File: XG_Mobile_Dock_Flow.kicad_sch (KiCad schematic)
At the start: 22 parts, among them J1 5-1775443-8, J13 39300240, J14 469911008, J17 8730, J2 20455-040E-76, J3 20455-040E-76, J4 3-2362375-4, J5 USB_C_Receptacle, SW1 SW_Push, U1 DS160PR410RNQR, U2 DS160PR410RNQR

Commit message: added more schematic
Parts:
- added C1, C10, C11, C12, C13, C14, C15, C16, C2, C3, C4, C5, C6, C7, C8, C9: 0.22μF, Capacitor_SMD:C_0201_0603Metric, symbol Device:C
- added C17, C18, C19, C20, C22, C23, C24, C25: 0.1μF, Capacitor_SMD:C_0201_0603Metric, symbol Device:C
- added C21, C26: 1μF, Capacitor_SMD:C_0201_0603Metric, symbol Device:C
- added R64, R65: 1k, Resistor_SMD:R_0402_1005Metric, symbol Device:R
- added R66, R67, R68, R69: 59k, Resistor_SMD:R_0402_1005Metric, symbol Device:R
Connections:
- net U1_VDD0 is gone; now on net +3V3: U1.31 (VDD)
- net U1_VDD1 is gone; now on net +3V3: U1.34 (VDD)
- net U1_VDD2 is gone; now on net +3V3: U1.35 (VDD)
- net U1_VDD3 is gone; now on net +3V3: U1.38 (VDD)
- net U2_VDD0 is gone; now on net +3V3: U2.31 (VDD)
- net U2_VDD1 is gone; now on net +3V3: U2.34 (VDD)
- net U2_VDD2 is gone; now on net +3V3: U2.35 (VDD)
- net U2_VDD3 is gone; now on net +3V3: U2.38 (VDD)
- net +3V3: now also C17.2, C18.2, C19.2, C20.2, C21.2, C22.2, C23.2, C24.2, C25.2, C26.2
- net GND: now also U1.21 (PWDN1), U1.25 (PWDN2), U1.41 (GND), U2.21 (PWDN1), U2.25 (PWDN2), U2.41 (GND), C17.1, C18.1, C19.1, C20.1, C21.1, C22.1, C23.1, C24.1, C25.1, C26.1, R64.1, R65.1, R66.1, R67.1, R68.1, R69.1
- net HSO0N: now also C2.2
- net HSO0P: now also C1.2
- net HSO1N: now also C4.2
- net HSO1P: now also C3.2
- net HSO2N: now also C6.2
- net HSO2P: now also C5.2
- net HSO3N: now also C8.2
- net HSO3P: now also C7.2
- net HSO4N: now also C10.2
- net HSO4P: now also C9.2
- net HSO5N: now also C12.2
- net HSO5P: now also C11.2
- net HSO6N: now also C14.2
- net HSO6P: now also C13.2
- net HSO7N: now also C16.2
- net HSO7P: now also C15.2
- net HSOT0N: now also C2.1
- net HSOT0P: now also C1.1
- net HSOT1N: now also C4.1
- net HSOT1P: now also C3.1
- net HSOT2N: now also C6.1
- net HSOT2P: now also C5.1
- net HSOT3N: now also C8.1
- net HSOT3P: now also C7.1
- net HSOT4N: now also C10.1
- net HSOT4P: now also C9.1
- net HSOT5N: now also C12.1
- net HSOT5P: now also C11.1
- net HSOT6N: now also C14.1
- net HSOT6P: now also C13.1
- net HSOT7N: now also C16.1
- net HSOT7P: now also C15.1
- net at U2.2 (EN_SMB): now also R65.2
- net at U2.6 (EQ1_ADDR1): now also R66.2
- net at U2.7 (EQ0_ADDR0): now also R67.2
- net at U1.2 (EN_SMB): now also R64.2
- net at U1.6 (EQ1_ADDR1): now also R68.2
- net at U1.7 (EQ0_ADDR0): now also R69.2
- no-connect marks 0 -> 14
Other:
- moved on the sheet: J14, U2

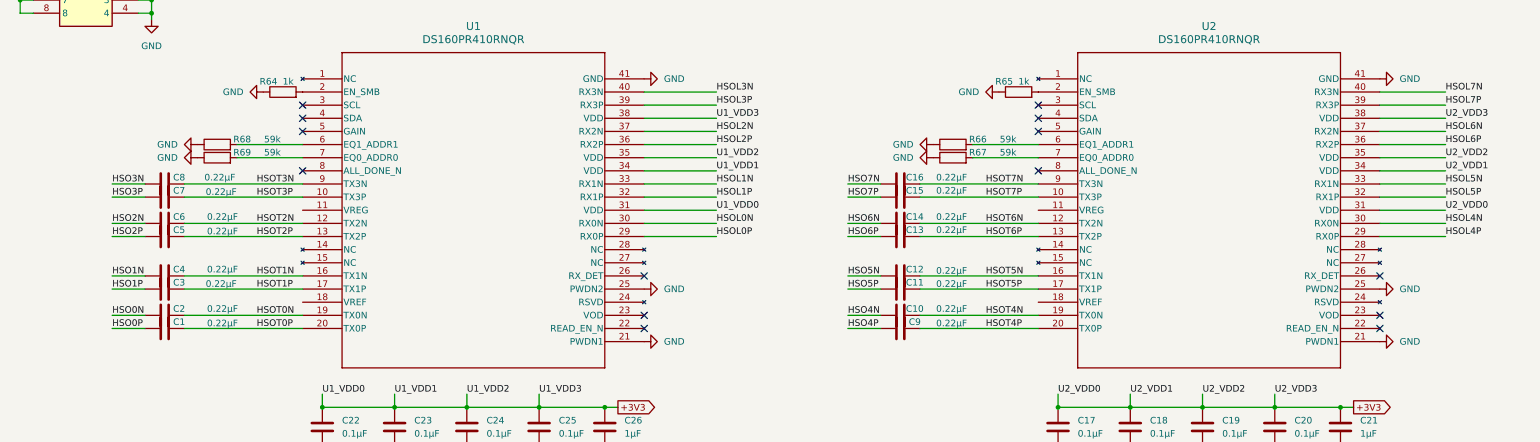
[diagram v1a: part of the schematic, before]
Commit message: added more things to the schematic for proper wiring of open pins with high and low resistors
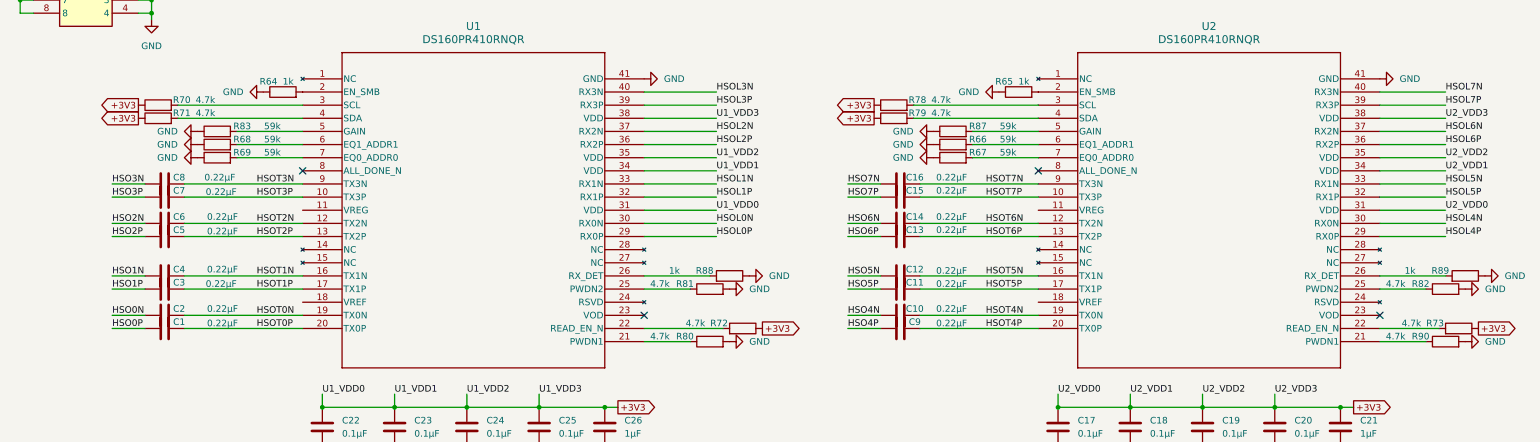
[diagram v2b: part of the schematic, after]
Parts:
- added R70, R71, R72, R73, R78, R79, R80, R81, R82, R90: 4.7k, Resistor_SMD:R_0402_1005Metric, symbol Device:R
- added R83, R87: 59k, Resistor_SMD:R_0402_1005Metric, symbol Device:R
- added R88, R89: 1k, Resistor_SMD:R_0402_1005Metric, symbol Device:R
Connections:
- net +3V3: now also R70.1, R71.1, R72.1, R73.1, R78.1, R79.1
- net GND: now also R80.2, R81.2, R82.2, R83.1, R87.1, R88.1, R89.1, R90.2; no longer U1.21 (PWDN1), U1.25 (PWDN2), U2.21 (PWDN1), U2.25 (PWDN2)
- net at U2.22 (READ_EN_N): now also R73.2
- net at U2.26 (RX_DET): now also R89.2
- net at U2.3 (SCL): now also R78.2
- net at U2.4 (SDA): now also R79.2
- net at U2.5 (GAIN): now also R87.2
- net at U1.22 (READ_EN_N): now also R72.2
- net at U1.26 (RX_DET): now also R88.2
- net at U1.3 (SCL): now also R70.2
- net at U1.4 (SDA): now also R71.2
- net at U1.5 (GAIN): now also R83.2
- new net: R82.1, U2.25 (PWDN2)
- new net: R90.1, U2.21 (PWDN1)
- new net: R80.1, U1.21 (PWDN1)
- new net: R81.1, U1.25 (PWDN2)
- no-connect marks 14 -> 4

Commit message: almost finished everything
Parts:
- added C27, C28, C29, C30: 0.1μF, Capacitor_SMD:C_0201_0603Metric, symbol Device:C
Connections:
- net GND: now also C27.2, C28.2, C29.2, C30.2
- net at U2.11 (VREG): now also C30.1
- net at U2.18 (VREF): now also C29.1
- net at U1.11 (VREG): now also C27.1
- net at U1.18 (VREF): now also C28.1
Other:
- moved on the sheet: C10, C11, C12, C13, C14, C15, C16, C17, C18, C19, C20, C21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

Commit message: more preparations for building the board
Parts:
- C1, C10, C11, C12, C13, C14, C15, C16, C2, C3, C4, C5, C6, C7, C8, C9: value 0.22μF -> 220nF
- C17, C18, C19, C20, C22, C23, C24, C25: value 0.1μF -> 100nF
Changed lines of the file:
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@@
 			)
 		)
-		(property "Value" "0.22μF"
+		(property "Value" "220nF"
 			(at 210.566 235.204 90)
 			(effects
@@
 			)
 		)
-		(property "Value" "0.22μF"
+		(property "Value" "220nF"
 			(at 62.992 217.424 90)
 			(effects
@@
 			)
 		)
-		(property "Value" "0.22μF"
+		(property "Value" "220nF"
 			(at 63.246 242.824 90)
 			(effects
@@
 			)
 		)
-		(property "Value" "0.22μF"
+		(property "Value" "220nF"
 			(at 210.566 240.03 90)
 			(effects
@@
 			)
 		)
-		(property "Value" "0.22μF"
+		(property "Value" "220nF"
 			(at 63.246 222.25 90)
 			(effects
@@
 			)
 		)
-		(property "Value" "0.22μF"
+		(property "Value" "220nF"
 			(at 210.566 242.824 90)
 			(effects
@@
 			)
 		)
-		(property "Value" "0.1μF"
+		(property "Value" "100nF"
 			(at 100.33 264.1599 0)
 			(effects
@@
 			)
 		)
-		(property "Value" "0.1μF"
+		(property "Value" "100nF"
 			(at 114.3 264.1599 0)
 			(effects
@@
 			)
 		)
-		(property "Value" "0.1μF"
+		(property "Value" "100nF"
 			(at 128.27 264.1599 0)
 			(effects
@@
 			)
 		)
-		(property "Value" "0.1μF"
+		(property "Value" "100nF"
 			(at 276.86 264.1599 0)
 			(effects
@@
 			)
 		)
-		(property "Value" "0.22μF"
+		(property "Value" "220nF"
 			(at 210.566 222.25 90)
 			(effects
@@
 			)
 		)
-		(property "Value" "0.1μF"
+		(property "Value" "100nF"
 			(at 234.95 264.1599 0)
 			(effects
@@
 			)
 		)
-		(property "Value" "0.22μF"
+		(property "Value" "220nF"
 			(at 210.566 224.79 90)
 			(effects
@@
 			)
 		)
-		(property "Value" "0.22μF"
+		(property "Value" "220nF"
 			(at 62.738 214.63 90)
 			(effects
@@
 			)
 		)
-		(property "Value" "0.1μF"
+		(property "Value" "100nF"
 			(at 262.89 264.1599 0)
 			(effects
@@
 			)
 		)
-		(property "Value" "0.1μF"
+		(property "Value" "100nF"
 			(at 86.36 264.1599 0)
 			(effects
@@
 			)
 		)
-		(property "Value" "0.1μF"
+		(property "Value" "100nF"
 			(at 248.92 264.1599 0)
 			(effects
@@
 			)
 		)
-		(property "Value" "0.22μF"
+		(property "Value" "220nF"
 			(at 210.566 232.664 90)
 			(effects
@@
 			)
 		)
-		(property "Value" "0.22μF"
+		(property "Value" "220nF"
 			(at 63.246 240.03 90)
 			(effects
@@
 			)
 		)
-		(property "Value" "0.22μF"
+		(property "Value" "220nF"
 			(at 210.566 217.17 90)
 			(effects
@@
 			)
 		)
-		(property "Value" "0.22μF"
+		(property "Value" "220nF"
 			(at 63.246 232.41 90)
 			(effects
@@
 			)
 		)
-		(property "Value" "0.22μF"
+		(property "Value" "220nF"
 			(at 62.992 235.204 90)
 			(effects
@@
 			)
 		)
-		(property "Value" "0.22μF"
+		(property "Value" "220nF"
 			(at 63.246 225.044 90)
 			(effects
@@
 			)
 		)
-		(property "Value" "0.22μF"
+		(property "Value" "220nF"
 			(at 210.566 214.63 90)
 			(effects

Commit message: fixed part numbers
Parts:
- C1, C10, C11, C12, C13, C14, C15, C16, C2, C3, C4, C5, C6, C7, C8, C9: LCSC (none) -> C7503500; Part_Number (none) -> CGA0603X7R224K160JT
- C17, C18, C19, C20, C22, C23, C24, C25: LCSC (none) -> C45000; Part_Number (none) -> GRM188R71C104KA01D
- C21, C26: LCSC (none) -> C1592; Part_Number (none) -> CL10A105KO8NNNC
- C27, C28, C29, C30: value 0.1μF -> 100nF; LCSC (none) -> C45000; Part_Number (none) -> GRM188R71C104KA01D
- R64, R65, R88, R89: LCSC C25744 -> C11702; Part_Number 0402WGF1002TCE -> 0402WGF1001TCE
- R66, R67, R68, R69, R83, R87: LCSC C25744 -> C32297; Part_Number 0402WGF1002TCE -> 0402WGF5902TCE
- R70, R71, R72, R73, R78, R79, R80, R81, R82, R90: LCSC C25744 -> C25900; Part_Number 0402WGF1002TCE -> 0402WGF4701TCE
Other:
- note added: "100nF GRM188R71C104KA01D MfPart C45000 LCSC 1k 0402WGF1001TCE MfPart C11702 LCSC 220nF CGA0603X7R224K160JT MfPart C7503500 LCSC 1uf CL10A105KO8NNNC MfPart C1592 LCSC 59k 0402WGF5902TCE MfPart C32297 LCSC 4.7k 0402WGF4701TCE MfPart C25900 LCSC"
- moved on the sheet: C1, C2, C22, C23, C24, C25, C26, C27, C28, C3, C4, C5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

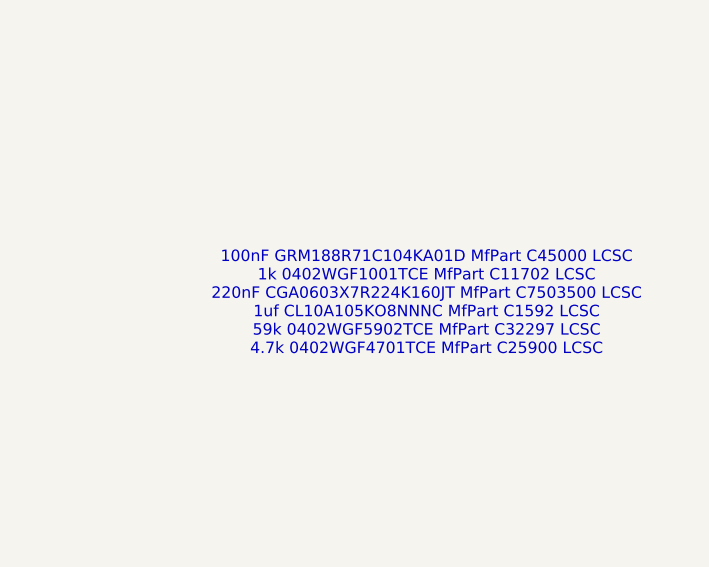
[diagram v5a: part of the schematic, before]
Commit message: fixed part numbers
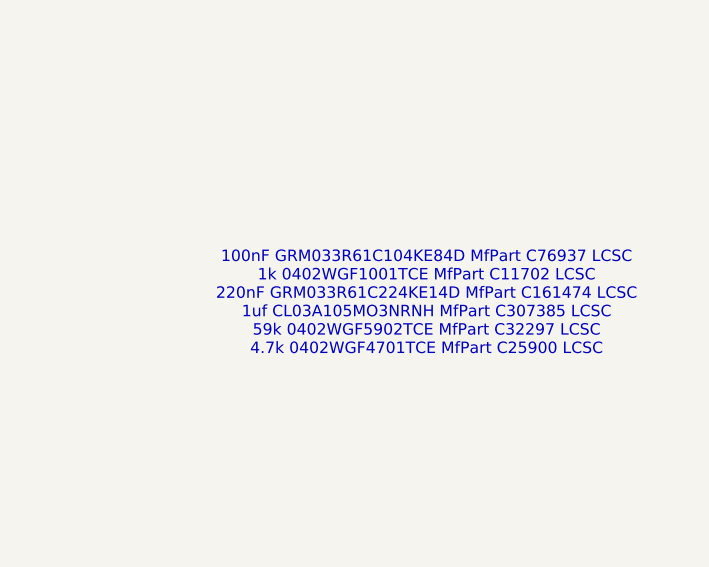
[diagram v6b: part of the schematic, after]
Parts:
- C1, C10, C11, C12, C13, C14, C15, C16, C2, C3, C4, C5, C6, C7, C8, C9: LCSC C7503500 -> C161474; Part_Number CGA0603X7R224K160JT -> GRM033R61C224KE14D
- C17, C18, C20, C22, C23, C24, C25, C27, C28, C29, C30: LCSC C45000 -> C76937; Part_Number GRM188R71C104KA01D -> GRM033R61C104KE84D
- C19: LCSC C45000 -> C76937
- C21, C26: LCSC C1592 -> C307385; Part_Number CL10A105KO8NNNC -> CL03A105MO3NRNH
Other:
- note added: "100nF GRM033R61C104KE84D MfPart C76937 LCSC 1k 0402WGF1001TCE MfPart C11702 LCSC 220nF GRM033R61C224KE14D MfPart C161474 LCSC 1uf CL03A105MO3NRNH MfPart C307385 LCSC 59k 0402WGF5902TCE MfPart C32297 LCSC 4.7k 0402WGF4701TCE MfPart C25900 LCSC"
- note removed: "100nF GRM188R71C104KA01D MfPart C45000 LCSC 1k 0402WGF1001TCE MfPart C11702 LCSC 220nF CGA0603X7R224K160JT MfPart C7503500 LCSC 1uf CL10A105KO8NNNC MfPart C1592 LCSC 59k 0402WGF5902TCE MfPart C32297 LCSC 4.7k 0402WGF4701TCE MfPart C25900 LCSC"
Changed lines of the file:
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@@
 	(generator_version "9.0")
 	(paper "A3")
-	(text "100nF GRM188R71C104KA01D MfPart C45000 LCSC\n1k 0402WGF1001TCE MfPart C11702 LCSC\n220nF CGA0603X7R224K160JT MfPart C7503500 LCSC\n1uf CL10A105KO8NNNC MfPart C1592 LCSC \n59k 0402WGF5902TCE MfPart C32297 LCSC\n4.7k 0402WGF4701TCE MfPart C25900 LCSC"
+	(text "100nF GRM033R61C104KE84D MfPart C76937 LCSC\n1k 0402WGF1001TCE MfPart C11702 LCSC\n220nF GRM033R61C224KE14D MfPart C161474 LCSC\n1uf CL03A105MO3NRNH MfPart C307385 LCSC \n59k 0402WGF5902TCE MfPart C32297 LCSC\n4.7k 0402WGF4701TCE MfPart C25900 LCSC"
 		(exclude_from_sim no)
 		(at 370.586 223.774 0)
@@
 			)
 		)
-		(property "Part_Number" "CGA0603X7R224K160JT"
+		(property "Part_Number" "GRM033R61C224KE14D"
 			(at 200.66 236.22 90)
 			(effects
@@
 			)
 		)
-		(property "LCSC" "C7503500"
+		(property "LCSC" "C161474"
 			(at 200.66 236.22 90)
 			(effects
@@
 			)
 		)
-		(property "Part_Number" "GRM188R71C104KA01D"
+		(property "Part_Number" "GRM033R61C104KE84D"
 			(at 185.42 238.76 90)
 			(effects
@@
 			)
 		)
-		(property "LCSC" "C45000"
+		(property "LCSC" "C76937"
 			(at 185.42 238.76 90)
 			(effects
@@
 			)
 		)
-		(property "Part_Number" "CGA0603X7R224K160JT"
+		(property "Part_Number" "GRM033R61C224KE14D"
 			(at 40.64 223.52 90)
 			(effects
@@
 			)
 		)
-		(property "LCSC" "C7503500"
+		(property "LCSC" "C161474"
 			(at 40.64 223.52 90)
 			(effects
@@
 			)
 		)
-		(property "Part_Number" "CGA0603X7R224K160JT"
+		(property "Part_Number" "GRM033R61C224KE14D"
 			(at 40.64 248.92 90)
 			(effects
@@
 			)
 		)
-		(property "LCSC" "C7503500"
+		(property "LCSC" "C161474"
 			(at 40.64 248.92 90)
 			(effects
@@
 			)
 		)
-		(property "Part_Number" "CGA0603X7R224K160JT"
+		(property "Part_Number" "GRM033R61C224KE14D"
 			(at 200.66 241.3 90)
 			(effects
@@
 			)
 		)
-		(property "LCSC" "C7503500"
+		(property "LCSC" "C161474"
 			(at 200.66 241.3 90)
 			(effects
@@
 			)
 		)
-		(property "Part_Number" "CGA0603X7R224K160JT"
+		(property "Part_Number" "GRM033R61C224KE14D"
 			(at 40.64 228.6 90)
 			(effects
@@
 			)
 		)
-		(property "LCSC" "C7503500"
+		(property "LCSC" "C161474"
 			(at 40.64 228.6 90)
 			(effects
@@
 			)
 		)
-		(property "Part_Number" "CGA0603X7R224K160JT"
+		(property "Part_Number" "GRM033R61C224KE14D"
 			(at 200.66 243.84 90)
 			(effects
@@
 			)
 		)
-		(property "LCSC" "C7503500"
+		(property "LCSC" "C161474"
 			(at 200.66 243.84 90)
 			(effects
@@
 			)
 		)
-		(property "Part_Number" "GRM188R71C104KA01D"
+		(property "Part_Number" "GRM033R61C104KE84D"
 			(at 90.17 267.97 0)
 			(effects
@@
 			)
 		)
-		(property "LCSC" "C45000"
+		(property "LCSC" "C76937"
 			(at 90.17 267.97 0)
 			(effects
@@
 			)
 		)
-		(property "Part_Number" "GRM188R71C104KA01D"
+		(property "Part_Number" "GRM033R61C104KE84D"
 			(at 104.14 267.97 0)
 			(effects
@@
 			)
 		)
-		(property "LCSC" "C45000"
+		(property "LCSC" "C76937"
 			(at 104.14 267.97 0)
 			(effects
@@
 			)
 		)
-		(property "Part_Number" "GRM188R71C104KA01D"
+		(property "Part_Number" "GRM033R61C104KE84D"
 			(at 118.11 267.97 0)
 			(effects
@@
 			)
 		)
-		(property "LCSC" "C45000"
+		(property "LCSC" "C76937"
 			(at 118.11 267.97 0)
 			(effects
@@
 			)
 		)
-		(property "Part_Number" "GRM188R71C104KA01D"
+		(property "Part_Number" "GRM033R61C104KE84D"
 			(at 273.05 262.89 0)
 			(effects
@@
 			)
 		)
-		(property "LCSC" "C45000"
+		(property "LCSC" "C76937"
 			(at 273.05 262.89 0)
 			(effects
@@
 			)
 		)
-		(property "Part_Number" "CGA0603X7R224K160JT"
+		(property "Part_Number" "GRM033R61C224KE14D"
 			(at 200.66 223.52 90)
 			(effects
@@
 			)
 		)
-		(property "LCSC" "C7503500"
+		(property "LCSC" "C161474"
 			(at 200.66 223.52 90)
 			(effects
@@
 			)
 		)
-		(property "Part_Number" "GRM188R71C104KA01D"
+		(property "Part_Number" "GRM033R61C104KE84D"
 			(at 231.14 262.89 0)
 			(effects
@@
 			)
 		)
-		(property "LCSC" "C45000"
+		(property "LCSC" "C76937"
 			(at 231.14 262.89 0)
 			(effects
@@
 			)
 		)
-		(property "Part_Number" "CGA0603X7R224K160JT"
+		(property "Part_Number" "GRM033R61C224KE14D"
 			(at 200.66 226.06 90)
 			(effects
@@
 			)
 		)
-		(property "LCSC" "C7503500"
+		(property "LCSC" "C161474"
 			(at 200.66 226.06 90)
 			(effects
@@
 			)
 		)
-		(property "Part_Number" "CGA0603X7R224K160JT"
+		(property "Part_Number" "GRM033R61C224KE14D"
 			(at 40.64 220.98 90)
 			(effects
@@
 			)
 		)
-		(property "LCSC" "C7503500"
+		(property "LCSC" "C161474"
 			(at 40.64 220.98 90)
 			(effects
@@
 			)
 		)
-		(property "LCSC" "C45000"
+		(property "LCSC" "C76937"
 			(at 259.08 262.89 0)
 			(effects
@@
 			)
 		)
-		(property "Part_Number" "CL10A105KO8NNNC"
+		(property "Part_Number" "CL03A105MO3NRNH"
 			(at 285.75 262.89 0)
 			(effects
@@
 			)
 		)
-		(property "LCSC" "C1592"
+		(property "LCSC" "C307385"
 			(at 285.75 262.89 0)
 			(effects
@@
 			)
 		)
-		(property "Part_Number" "GRM188R71C104KA01D"
+		(property "Part_Number" "GRM033R61C104KE84D"
 			(at 25.4 226.06 90)
 			(effects
@@
 			)
 		)
-		(property "LCSC" "C45000"
+		(property "LCSC" "C76937"
 			(at 25.4 226.06 90)
 			(effects
@@
 			)
 		)
-		(property "Part_Number" "GRM188R71C104KA01D"
+		(property "Part_Number" "GRM033R61C104KE84D"
 			(at 76.2 267.97 0)
 			(effects
@@
 			)
 		)
-		(property "LCSC" "C45000"
+		(property "LCSC" "C76937"
 			(at 76.2 267.97 0)
 			(effects
@@
 			)
 		)
-		(property "Part_Number" "GRM188R71C104KA01D"
+		(property "Part_Number" "GRM033R61C104KE84D"
 			(at 245.11 262.89 0)
 			(effects
@@
 			)
 		)
-		(property "LCSC" "C45000"
+		(property "LCSC" "C76937"
 			(at 245.11 262.89 0)
 			(effects
@@
 			)
 		)
-		(property "Part_Number" "CGA0603X7R224K160JT"
+		(property "Part_Number" "GRM033R61C224KE14D"
 			(at 200.66 233.68 90)
 			(effects
@@
 			)
 		)
-		(property "LCSC" "C7503500"
+		(property "LCSC" "C161474"
 			(at 200.66 233.68 90)
 			(effects
@@
 			)
 		)
-		(property "Part_Number" "CL10A105KO8NNNC"
+		(property "Part_Number" "CL03A105MO3NRNH"
 			(at 130.81 267.97 0)
 			(effects
@@
 			)
 		)
-		(property "LCSC" "C1592"
+		(property "LCSC" "C307385"
 			(at 130.81 267.97 0)
 			(effects
@@
 			)
 		)
-		(property "Part_Number" "CGA0603X7R224K160JT"
+		(property "Part_Number" "GRM033R61C224KE14D"
 			(at 40.64 246.38 90)
 			(effects
@@
 			)
 		)
-		(property "LCSC" "C7503500"
+		(property "LCSC" "C161474"
 			(at 40.64 246.38 90)
 			(effects
@@
 			)
 		)
-		(property "Part_Number" "GRM188R71C104KA01D"
+		(property "Part_Number" "GRM033R61C104KE84D"
 			(at 25.4 243.84 90)
 			(effects
@@
 			)
 		)
-		(property "LCSC" "C45000"
+		(property "LCSC" "C76937"
 			(at 25.4 243.84 90)
 			(effects
@@
 			)
 		)
-		(property "Part_Number" "CGA0603X7R224K160JT"
+		(property "Part_Number" "GRM033R61C224KE14D"
 			(at 200.66 218.44 90)
 			(effects
@@
 			)
 		)
-		(property "LCSC" "C7503500"
+		(property "LCSC" "C161474"
 			(at 200.66 218.44 90)
 			(effects
@@
 			)
 		)
-		(property "Part_Number" "CGA0603X7R224K160JT"
+		(property "Part_Number" "GRM033R61C224KE14D"
 			(at 40.64 238.76 90)
 			(effects
@@
 			)
 		)
-		(property "LCSC" "C7503500"
+		(property "LCSC" "C161474"
 			(at 40.64 238.76 90)
 			(effects
@@
 			)
 		)
-		(property "Part_Number" "CGA0603X7R224K160JT"
+		(property "Part_Number" "GRM033R61C224KE14D"
 			(at 40.64 241.3 90)
 			(effects
@@
 			)
 		)
-		(property "LCSC" "C7503500"
+		(property "LCSC" "C161474"
 			(at 40.64 241.3 90)
 			(effects
@@
 			)
 		)
-		(property "Part_Number" "GRM188R71C104KA01D"
+		(property "Part_Number" "GRM033R61C104KE84D"
 			(at 185.42 220.98 90)
 			(effects
@@
 			)
 		)
-		(property "LCSC" "C45000"
+		(property "LCSC" "C76937"
 			(at 185.42 220.98 90)
 			(effects
@@
 			)
 		)
-		(property "Part_Number" "CGA0603X7R224K160JT"
+		(property "Part_Number" "GRM033R61C224KE14D"
 			(at 40.64 231.14 90)
 			(effects
@@
 			)
 		)
-		(property "LCSC" "C7503500"
+		(property "LCSC" "C161474"
 			(at 40.64 231.14 90)
 			(effects
@@
 			)
 		)
-		(property "Part_Number" "CGA0603X7R224K160JT"
+		(property "Part_Number" "GRM033R61C224KE14D"
 			(at 200.66 215.9 90)
 			(effects
@@
 			)
 		)
-		(property "LCSC" "C7503500"
+		(property "LCSC" "C161474"
 			(at 200.66 215.9 90)
 			(effects
